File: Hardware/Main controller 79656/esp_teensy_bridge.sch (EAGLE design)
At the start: 105 parts, among them IC2 PBQ79656PAPTQ1, Q5 VISHAY_SIS862DN-T1-GE3VISHAY_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, Q6 VISHAY_SIS862DN-T1-GE3VISHAY_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, Q7 VISHAY_SIS862DN-T1-GE3VISHAY_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, Q8 VISHAY_SIS862DN-T1-GE3VISHAY_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, T2 PBHV8115X, 115, U1 MCP2562-E/SN, U2 ESP32-DEVKITC-32D, X1 5566-12

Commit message: level shiffft
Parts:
- added U$1: TXB0108PWSMD, TB0108:TXB0108PWSMD
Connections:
- new net RX_SHFT: U$1.B2, U$3.34-RX8
- new net TX_SHFT: U$1.B1, U$3.35/TX8
- net 3V3: now also U$1.VCCA
- net GND: now also U$1.GND
- net RX_BQ: now also U$1.A2; no longer U$3.35/TX8
- net TX_BQ: now also U$1.A1; no longer U$3.34-RX8
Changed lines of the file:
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@@
 <part name="R4" library="rcl" library_urn="urn:adsk.eagle:library:334" deviceset="R-US_" device="R0805" package3d_urn="urn:adsk.eagle:package:23553/2"/>
 <part name="R9" library="rcl" library_urn="urn:adsk.eagle:library:334" deviceset="R-US_" device="R0805" package3d_urn="urn:adsk.eagle:package:23553/2"/>
+<part name="U$1" library="TB0108" deviceset="TXB0108PW" device="SMD"/>
 </parts>
 <sheets>
@@
 <attribute name="NAME" x="-118.3386" y="-163.83" size="1.778" layer="95" rot="R90"/>
 <attribute name="VALUE" x="-113.538" y="-163.83" size="1.778" layer="96" rot="R90"/>
+</instance>
+<instance part="U$1" gate="G$1" x="73.66" y="-63.5" smashed="yes" rot="R270">
+<attribute name="NAME" x="73.66" y="-60.96" size="1.27" layer="95"/>
+<attribute name="VALUE" x="88.9" y="-121.92" size="1.27" layer="96" rot="R180"/>
 </instance>
 </instances>
@@
 <junction x="-114.3" y="-193.04"/>
 </segment>
+<segment>
+<pinref part="U$1" gate="G$1" pin="GND"/>
+<wire x1="93.98" y1="-114.3" x2="99.06" y2="-114.3" width="0.1524" layer="91"/>
+<label x="99.06" y="-114.3" size="1.778" layer="95"/>
+</segment>
 </net>
 <net name="TX_ESP" class="0">
@@
 <pinref part="C7" gate="G$1" pin="1"/>
 </segment>
+<segment>
+<pinref part="U$1" gate="G$1" pin="VCCA"/>
+<wire x1="68.58" y1="-73.66" x2="63.5" y2="-73.66" width="0.1524" layer="91"/>
+<label x="55.88" y="-73.66" size="1.778" layer="95"/>
+</segment>
 </net>
 <net name="CRX" class="0">
@@
 <net name="TX_BQ" class="0">
 <segment>
-<pinref part="U$3" gate="G$1" pin="34-RX8"/>
-<wire x1="96.52" y1="78.74" x2="101.6" y2="78.74" width="0.1524" layer="91"/>
-<label x="99.06" y="78.74" size="1.778" layer="95"/>
-</segment>
-<segment>
 <pinref part="IC2" gate="G$1" pin="TX"/>
 <wire x1="25.4" y1="-165.1" x2="30.48" y2="-165.1" width="0.1524" layer="91"/>
 <label x="27.94" y="-165.1" size="1.778" layer="95"/>
 </segment>
+<segment>
+<pinref part="U$1" gate="G$1" pin="A1"/>
+<wire x1="68.58" y1="-68.58" x2="63.5" y2="-68.58" width="0.1524" layer="91"/>
+<label x="55.88" y="-68.58" size="1.778" layer="95"/>
+</segment>
 </net>
 <net name="RX_BQ" class="0">
-<segment>
-<pinref part="U$3" gate="G$1" pin="35/TX8"/>
-<wire x1="96.52" y1="76.2" x2="101.6" y2="76.2" width="0.1524" layer="91"/>
-<label x="99.06" y="76.2" size="1.778" layer="95"/>
-</segment>
 <segment>
 <pinref part="IC2" gate="G$1" pin="RX"/>
 <wire x1="25.4" y1="-167.64" x2="30.48" y2="-167.64" width="0.1524" layer="91"/>
 <label x="27.94" y="-167.64" size="1.778" layer="95"/>
+</segment>
+<segment>
+<pinref part="U$1" gate="G$1" pin="A2"/>
+<wire x1="68.58" y1="-78.74" x2="63.5" y2="-78.74" width="0.1524" layer="91"/>
+<label x="55.88" y="-78.74" size="1.778" layer="95"/>
 </segment>
 </net>
@@
 </segment>
 </net>
+<net name="RX_SHFT" class="0">
+<segment>
+<pinref part="U$3" gate="G$1" pin="34-RX8"/>
+<wire x1="96.52" y1="78.74" x2="101.6" y2="78.74" width="0.1524" layer="91"/>
+<label x="101.6" y="78.74" size="1.778" layer="95"/>
+</segment>
+<segment>
+<pinref part="U$1" gate="G$1" pin="B2"/>
+<wire x1="93.98" y1="-78.74" x2="99.06" y2="-78.74" width="0.1524" layer="91"/>
+<label x="99.06" y="-78.74" size="1.778" layer="95"/>
+</segment>
+</net>
+<net name="TX_SHFT" class="0">
+<segment>
+<pinref part="U$3" gate="G$1" pin="35/TX8"/>
+<wire x1="96.52" y1="76.2" x2="101.6" y2="76.2" width="0.1524" layer="91"/>
+<label x="101.6" y="76.2" size="1.778" layer="95"/>
+</segment>
+<segment>
+<pinref part="U$1" gate="G$1" pin="B1"/>
+<wire x1="93.98" y1="-68.58" x2="99.06" y2="-68.58" width="0.1524" layer="91"/>
+<label x="99.06" y="-68.58" size="1.778" layer="95"/>
+</segment>
+</net>

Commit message: Late night mainboard layout
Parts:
- removed CCB0-1, CCB1-1, CCB2-1, CCB3-1: 0.47uf, rcl:C-EUC0603
- removed GNDH: (no value), wirepad:SMD5
- removed RCB0-1, RCB1-1, RCB2-1, RCB3-1, RCB4-1: 10, rcl:R-US_R1210
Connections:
- removed net BATC-1: RNPN-1.2
- removed net CB0-1: CCB0-1.2, IC2.CB0, RCB0-1.2
- removed net CB1-1: CCB0-1.1, CCB1-1.2, IC2.CB1, RCB1-1.2
- removed net CB2-1: CCB1-1.1, CCB2-1.2, IC2.CB2, RCB2-1.2
- removed net CB3-1: CCB2-1.1, CCB3-1.2, IC2.CB3, RCB3-1.2
- removed net CB4-1: CCB10-1.1, CCB3-1.1, IC2.CB4, RCB4-1.2
- removed net N$125: IC2.COMLN
- removed net N$126: IC2.COMLP
- net 3V3: now also U$1.OE
- net 5V: now also U$1.VCCB
- net GND: no longer GNDH.P, RCB0-1.1
- net N$10: now also IC2.COMLN
- net N$49: now also IC2.COMLP
- net N$72: no longer RCB2-1.1
- net N$73: no longer RCB1-1.1
- net N$75: no longer RCB3-1.1
- net RX_BQ: now also U$1.B2; no longer U$1.A2
- net RX_SHFT: now also U$1.A1; no longer U$1.B2
- net TX_BQ: now also U$1.B1; no longer U$1.A1
- net TX_SHFT: now also U$1.A2; no longer U$1.B1
- net VC0-1: now also IC2.CB0
- net VC1-1: now also IC2.CB1
- net VC2-1: now also IC2.CB2
- net VC3-1: now also IC2.CB3
- net VC4-1: now also CCB10-1.1, IC2.CB4
- net VCC: now also RNPN-1.2; no longer RCB4-1.1

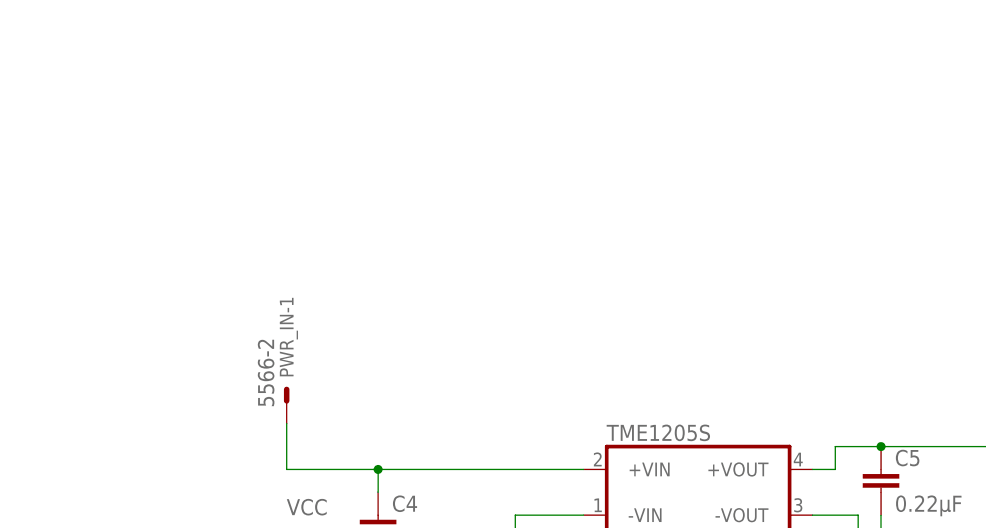
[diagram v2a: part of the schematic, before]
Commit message: dc dc buck converter replace
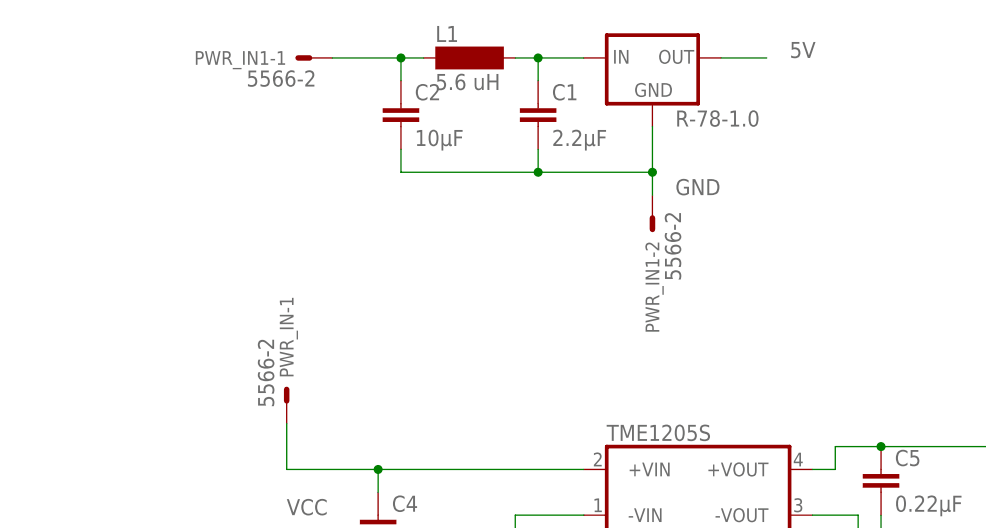
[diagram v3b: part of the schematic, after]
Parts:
- added C1: 2.2μF, rcl:C-EUC0603
- added C2: 10μF, rcl:C-EUC0603
- added L1: 5.6 uH, inductor-neosid:SD8
- added PWR_IN1: 5566-2, con-molex:5566-2
- added R-78-1.0: (no value), v-reg:78XXS
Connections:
- new net N$16: C1.1, L1.2, R-78-1.0.IN
- new net N$36: C2.1, L1.1, PWR_IN1-1.S
- net 5V: now also R-78-1.0.OUT
- net GND: now also C1.2, C2.2, PWR_IN1-2.S, R-78-1.0.GND
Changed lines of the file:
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@@
 <part name="R9" library="rcl" library_urn="urn:adsk.eagle:library:334" deviceset="R-US_" device="R0805" package3d_urn="urn:adsk.eagle:package:23553/2"/>
 <part name="U$1" library="TB0108" deviceset="TXB0108PW" device="SMD"/>
+<part name="R-78-1.0" library="v-reg" library_urn="urn:adsk.eagle:library:409" deviceset="78XXS" device="" package3d_urn="urn:adsk.eagle:package:30342/1"/>
+<part name="C1" library="rcl" library_urn="urn:adsk.eagle:library:334" deviceset="C-EU" device="C0603" package3d_urn="urn:adsk.eagle:package:23616/2" value="2.2μF"/>
+<part name="C2" library="rcl" library_urn="urn:adsk.eagle:library:334" deviceset="C-EU" device="C0603" package3d_urn="urn:adsk.eagle:package:23616/2" value="10μF"/>
+<part name="L1" library="inductor-neosid" library_urn="urn:adsk.eagle:library:241" deviceset="SD8" device="" package3d_urn="urn:adsk.eagle:package:14649/1" value="5.6 uH"/>
+<part name="PWR_IN1" library="con-molex" library_urn="urn:adsk.eagle:library:165" deviceset="5566-2" device="" package3d_urn="urn:adsk.eagle:package:8078583/1"/>
 </parts>
 <sheets>
@@
 <attribute name="NAME" x="73.66" y="-60.96" size="1.27" layer="95"/>
 <attribute name="VALUE" x="88.9" y="-121.92" size="1.27" layer="96" rot="R180"/>
+</instance>
+<instance part="R-78-1.0" gate="1" x="-35.56" y="160.02" smashed="yes">
+<attribute name="NAME" x="-33.02" y="152.4" size="1.778" layer="95"/>
+<attribute name="VALUE" x="-33.02" y="149.86" size="1.778" layer="96"/>
+</instance>
+<instance part="C1" gate="G$1" x="-48.26" y="154.94" smashed="yes">
+<attribute name="NAME" x="-46.736" y="155.321" size="1.778" layer="95"/>
+<attribute name="VALUE" x="-46.736" y="150.241" size="1.778" layer="96"/>
+</instance>
+<instance part="C2" gate="G$1" x="-63.5" y="154.94" smashed="yes">
+<attribute name="NAME" x="-61.976" y="155.321" size="1.778" layer="95"/>
+<attribute name="VALUE" x="-61.976" y="150.241" size="1.778" layer="96"/>
+</instance>
+<instance part="L1" gate="G$1" x="-55.88" y="160.02" smashed="yes">
+<attribute name="NAME" x="-59.69" y="161.798" size="1.778" layer="95"/>
+<attribute name="VALUE" x="-59.69" y="156.464" size="1.778" layer="96"/>
+</instance>
+<instance part="PWR_IN1" gate="-1" x="-73.66" y="160.02" smashed="yes" rot="R180">
+<attribute name="NAME" x="-76.2" y="160.782" size="1.524" layer="95" rot="R180"/>
+<attribute name="VALUE" x="-72.898" y="158.623" size="1.778" layer="96" rot="R180"/>
+</instance>
+<instance part="PWR_IN1" gate="-2" x="-35.56" y="142.24" smashed="yes" rot="R270">
+<attribute name="NAME" x="-36.322" y="139.7" size="1.524" layer="95" rot="R270"/>
+<attribute name="VALUE" x="-34.163" y="143.002" size="1.778" layer="96" rot="R270"/>
 </instance>
 </instances>
@@
 <label x="99.06" y="-114.3" size="1.778" layer="95"/>
 </segment>
+<segment>
+<pinref part="R-78-1.0" gate="1" pin="GND"/>
+<wire x1="-35.56" y1="152.4" x2="-35.56" y2="147.32" width="0.1524" layer="91"/>
+<wire x1="-35.56" y1="147.32" x2="-48.26" y2="147.32" width="0.1524" layer="91"/>
+<pinref part="C1" gate="G$1" pin="2"/>
+<wire x1="-48.26" y1="147.32" x2="-63.5" y2="147.32" width="0.1524" layer="91"/>
+<wire x1="-48.26" y1="149.86" x2="-48.26" y2="147.32" width="0.1524" layer="91"/>
+<junction x="-48.26" y="147.32"/>
+<pinref part="C2" gate="G$1" pin="2"/>
+<wire x1="-63.5" y1="149.86" x2="-63.5" y2="147.32" width="0.1524" layer="91"/>
+<pinref part="PWR_IN1" gate="-2" pin="S"/>
+<wire x1="-35.56" y1="147.32" x2="-35.56" y2="144.78" width="0.1524" layer="91"/>
+<junction x="-35.56" y="147.32"/>
+<label x="-33.02" y="144.78" size="1.778" layer="95"/>
+</segment>
 </net>
 <net name="TX_ESP" class="0">
@@
 <wire x1="93.98" y1="-73.66" x2="99.06" y2="-73.66" width="0.1524" layer="91"/>
 <label x="96.52" y="-73.66" size="1.778" layer="95"/>
+</segment>
+<segment>
+<pinref part="R-78-1.0" gate="1" pin="OUT"/>
+<wire x1="-27.94" y1="160.02" x2="-22.86" y2="160.02" width="0.1524" layer="91"/>
+<label x="-20.32" y="160.02" size="1.778" layer="95"/>
 </segment>
 </net>
@@
 </segment>
 </net>
+<net name="N$16" class="0">
+<segment>
+<pinref part="R-78-1.0" gate="1" pin="IN"/>
+<pinref part="C1" gate="G$1" pin="1"/>
+<wire x1="-48.26" y1="157.48" x2="-48.26" y2="160.02" width="0.1524" layer="91"/>
+<wire x1="-43.18" y1="160.02" x2="-48.26" y2="160.02" width="0.1524" layer="91"/>
+<pinref part="L1" gate="G$1" pin="2"/>
+<wire x1="-50.8" y1="160.02" x2="-48.26" y2="160.02" width="0.1524" layer="91"/>
+<junction x="-48.26" y="160.02"/>
+</segment>
+</net>
+<net name="N$36" class="0">
+<segment>
+<pinref part="C2" gate="G$1" pin="1"/>
+<wire x1="-63.5" y1="157.48" x2="-63.5" y2="160.02" width="0.1524" layer="91"/>
+<pinref part="L1" gate="G$1" pin="1"/>
+<wire x1="-63.5" y1="160.02" x2="-60.96" y2="160.02" width="0.1524" layer="91"/>
+<pinref part="PWR_IN1" gate="-1" pin="S"/>
+<wire x1="-63.5" y1="160.02" x2="-71.12" y2="160.02" width="0.1524" layer="91"/>
+<junction x="-63.5" y="160.02"/>
+</segment>
+</net>
